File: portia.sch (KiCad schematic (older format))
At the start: 60 parts, among them J1 USB_B_Micro, J11 Conn_01x02, J12 Conn_01x02, J13 Conn_01x02, J14 Conn_01x02, J2 Conn_02x04_Counter_Clockwise, J3 Conn_01x02, J4 Conn_01x02, J5 RASPBERRYPI-40-PIN-GPIO, J7 Conn_01x02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

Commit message: modified trace connections
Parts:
- removed D8: D, Diode_SMD:D_SOD-123F, symbol Device:D
- removed JP8, JP9: SolderJumper_2_Open, Jumper:SolderJumper-2_P1.3mm_Open_RoundedPad1.0x1.5mm, symbol Jumper:SolderJumper_2_Open
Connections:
- wire segments 221 -> 218
- no-connect marks 40 -> 42
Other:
- moved on the sheet: R16
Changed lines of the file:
@@
 EESchema Schematic File Version 4
-LIBS:esp32_io_board-cache
+LIBS:portia-cache
 EELAYER 26 0
 EELAYER END
@@
 	14950 7800 14600 7800
 $Comp
-L power:+3.3V #PWR0134
-U 1 1 5C5CAF79
-P 14150 7800
-F 0 "#PWR0134" H 14150 7650 50  0001 C CNN
-F 1 "+3.3V" V 14165 7928 50  0000 L CNN
-F 2 "" H 14150 7800 50  0001 C CNN
-F 3 "" H 14150 7800 50  0001 C CNN
-	1    14150 7800
-	0    -1   -1   0
-$EndComp
-$Comp
 L Mechanical:MountingHole H4
 U 1 1 5C6145C5
@@
 	1    0    0    -1
 $EndComp
-$Comp
-L Device:D D8
-U 1 1 5C220000
-P 14450 7800
-F 0 "D8" H 14450 7584 50  0000 C CNN
-F 1 "D" H 14450 7675 50  0000 C CNN
-F 2 "Diode_SMD:D_SOD-123F" H 14450 7800 50  0001 C CNN
-F 3 "~" H 14450 7800 50  0001 C CNN
-	1    14450 7800
-	-1   0    0    1
-$EndComp
-Wire Wire Line
-	14150 7800 14300 7800
 Wire Wire Line
 	13850 8550 13850 8100
@@
 	13550 9450 13400 9450
 Wire Wire Line
-	13400 9450 13400 8950
-Wire Wire Line
-	12300 8950 12700 8950
-Wire Wire Line
-	13450 9050 13450 9550
+	13400 9450 13400 9150
+Wire Wire Line
+	13450 9050 13450 9300
 Wire Wire Line
 	13450 9550 13550 9550
@@
 	-1   0    0    1
 $EndComp
-Connection ~ 13450 9050
 Wire Wire Line
 	13400 8950 13600 8950
-Connection ~ 13400 8950
 Wire Wire Line
 	13450 9050 13600 9050
@@
 Text Label 16450 9700 0    50   ~ 0
 id_sda
-$Comp
-L Jumper:SolderJumper_2_Open JP8
-U 1 1 5C387087
-P 13000 8950
-F 0 "JP8" H 12954 9018 50  0000 L CNN
-F 1 "SolderJumper_2_Open" H 14200 10850 50  0000 L CNN
-F 2 "Jumper:SolderJumper-2_P1.3mm_Open_RoundedPad1.0x1.5mm" H 13000 8950 50  0001 C CNN
-F 3 "~" H 13000 8950 50  0001 C CNN
-	1    13000 8950
-	-1   0    0    1
-$EndComp
-Wire Wire Line
-	13150 8950 13400 8950
-Wire Wire Line
-	13150 9050 13450 9050
-$Comp
-L Jumper:SolderJumper_2_Open JP9
-U 1 1 5C3A9876
-P 13000 9050
-F 0 "JP9" H 12954 9118 50  0000 L CNN
-F 1 "SolderJumper_2_Open" H 14200 10750 50  0000 L CNN
-F 2 "Jumper:SolderJumper-2_P1.3mm_Open_RoundedPad1.0x1.5mm" H 13000 9050 50  0001 C CNN
-F 3 "~" H 13000 9050 50  0001 C CNN
-	1    13000 9050
-	-1   0    0    1
-$EndComp
 NoConn ~ 15050 8300
 NoConn ~ 15050 8500
@@
 Connection ~ 13950 9800
 Wire Wire Line
-	13950 9800 13950 9950
+	13950 9800 13950 9900
 Wire Wire Line
 	13150 8850 14200 8850
@@
 	8300 7400 8300 7650
 Wire Wire Line
-	12700 8950 12700 9350
-Wire Wire Line
-	12300 9050 12800 9050
-Connection ~ 12700 8950
-Wire Wire Line
-	12700 8950 12850 8950
-Wire Wire Line
-	12800 9050 12800 9250
-Connection ~ 12800 9050
-Wire Wire Line
-	12800 9050 12850 9050
-$Comp
-L Device:R_Small R16
-U 1 1 5C2A3FD8
-P 12800 9350
-F 0 "R16" V 12604 9350 50  0000 C CNN
-F 1 "R_Small" V 12695 9350 50  0000 C CNN
-F 2 "Resistor_SMD:R_0603_1608Metric" H 12800 9350 50  0001 C CNN
-F 3 "~" H 12800 9350 50  0001 C CNN
-	1    12800 9350
-	-1   0    0    1
-$EndComp
-$Comp
-L Device:R_Small R15
-U 1 1 5C2EA332
-P 12700 9450
-F 0 "R15" V 12504 9450 50  0000 C CNN
-F 1 "R_Small" V 12595 9450 50  0000 C CNN
-F 2 "Resistor_SMD:R_0603_1608Metric" H 12700 9450 50  0001 C CNN
-F 3 "~" H 12700 9450 50  0001 C CNN
-	1    12700 9450
-	-1   0    0    1
-$EndComp
-Wire Wire Line
-	12550 9550 12550 9650
-Wire Wire Line
-	12700 9550 12550 9550
-Connection ~ 12550 9550
-Wire Wire Line
-	12800 9450 12800 9650
-Wire Wire Line
-	12800 9650 12550 9650
-Connection ~ 12550 9650
-Wire Wire Line
-	12550 9650 12550 9800
-Wire Wire Line
 	10950 7850 10950 7500
 Connection ~ 10950 7850
@@
 $EndComp
 $Comp
-L power:GND #PWR?
+L power:GND #PWR0119
 U 1 1 5C438DC8
 P 14450 9150
-F 0 "#PWR?" H 14450 8900 50  0001 C CNN
+F 0 "#PWR0119" H 14450 8900 50  0001 C CNN
 F 1 "GND" V 14455 9022 50  0000 R CNN
 F 2 "" H 14450 9150 50  0001 C CNN
@@
 Wire Wire Line
 	14350 9150 14450 9150
+$Comp
+L Device:R_Small R16
+U 1 1 5C2A3FD8
+P 13200 9300
+F 0 "R16" V 13004 9300 50  0000 C CNN
+F 1 "R_Small" V 13095 9300 50  0000 C CNN
+F 2 "Resistor_SMD:R_0603_1608Metric" H 13200 9300 50  0001 C CNN
+F 3 "~" H 13200 9300 50  0001 C CNN
+	1    13200 9300
+	0    -1   -1   0
+$EndComp
+$Comp
+L Device:R_Small R15
+U 1 1 5C2E4AA2
+P 13200 9150
+F 0 "R15" V 13004 9150 50  0000 C CNN
+F 1 "R_Small" V 13095 9150 50  0000 C CNN
+F 2 "Resistor_SMD:R_0603_1608Metric" H 13200 9150 50  0001 C CNN
+F 3 "~" H 13200 9150 50  0001 C CNN
+	1    13200 9150
+	0    -1   -1   0
+$EndComp
+Wire Wire Line
+	12550 9550 12550 9800
+Wire Wire Line
+	13300 9150 13400 9150
+Connection ~ 13400 9150
+Wire Wire Line
+	13400 9150 13400 8950
+Wire Wire Line
+	13300 9300 13450 9300
+Connection ~ 13450 9300
+Wire Wire Line
+	13450 9300 13450 9550
+Wire Wire Line
+	13100 9150 13050 9150
+Wire Wire Line
+	13100 9300 13050 9300
+Wire Wire Line
+	13050 9150 13050 9300
+Wire Wire Line
+	13050 9900 13950 9900
+Connection ~ 13050 9300
+Wire Wire Line
+	13050 9300 13050 9900
+Connection ~ 13950 9900
+Wire Wire Line
+	13950 9900 13950 9950
+NoConn ~ 12300 8950
+NoConn ~ 12300 9050
+$Comp
+L power:+3.3V #PWR0134
+U 1 1 5C5CAF79
+P 14600 7800
+F 0 "#PWR0134" H 14600 7650 50  0001 C CNN
+F 1 "+3.3V" V 14615 7928 50  0000 L CNN
+F 2 "" H 14600 7800 50  0001 C CNN
+F 3 "" H 14600 7800 50  0001 C CNN
+	1    14600 7800
+	0    -1   -1   0
+$EndComp
 $EndSCHEMATC

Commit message: resolved routing issue
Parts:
- J5: footprint SparkFun-Boards:2X20-SHROUDED -> Connector_PinSocket_2.54mm:PinSocket_2x20_P2.54mm_Vertical
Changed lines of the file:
@@
 F 0 "J5" H 15650 9865 50  0000 C CNN
 F 1 "RASPBERRYPI-40-PIN-GPIO" H 15650 9774 50  0000 C CNN
-F 2 "SparkFun-Boards:2X20-SHROUDED" H 15680 8750 20  0001 C CNN
+F 2 "Connector_PinSocket_2.54mm:PinSocket_2x20_P2.54mm_Vertical" H 15680 8750 20  0001 C CNN
 F 3 "" H 15650 8600 50  0001 C CNN
 	1    15650 8600

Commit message: redesign removed 40 pin header
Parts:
- removed J5: RASPBERRYPI-40-PIN-GPIO, Connector_PinSocket_2.54mm:PinSocket_2x20_P2.54mm_Vertical, symbol SparkFun-Boards:RASPBERRYPI-40-PIN-GPIO
- removed JP4, JP7: SolderJumper_2_Open, Jumper:SolderJumper-2_P1.3mm_Open_RoundedPad1.0x1.5mm, symbol Jumper:SolderJumper_2_Open
- removed R12, R15, R16: R_Small, Resistor_SMD:R_0603_1608Metric, symbol Device:R_Small
- removed U7: CAT24C256, Package_SO:SOIC-8-1EP_3.9x4.9mm_P1.27mm_EP2.35x2.35mm, symbol Memory_EEPROM:CAT24C256
- F1: footprint Fuse:Fuse_1812_4532Metric_Pad1.30x3.40mm_HandSolder -> Fuse:Fuse_1206_3216Metric_Pad1.42x1.75mm_HandSolder
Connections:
- net labels removed: id_clk, id_sda
- wire segments 218 -> 160
- no-connect marks 42 -> 26

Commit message: updated schematic redesign
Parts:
- removed J2: Conn_02x04_Counter_Clockwise, Connector_PinHeader_2.54mm:PinHeader_2x04_P2.54mm_Vertical, symbol Connector_Generic:Conn_02x04_Counter_Clockwise
- removed J4: Conn_01x02, Connector_PinHeader_2.54mm:PinHeader_1x02_P2.54mm_Vertical, symbol Connector_Generic:Conn_01x02
- removed SW2: Bootloader, Button_Switch_SMD:SW_SPST_EVPBF, symbol Switch:SW_Push
- added J10, J15, J2, J5, J6, J9: Conn_01x02, Connector_PinHeader_2.54mm:PinHeader_1x02_P2.54mm_Vertical, symbol Connector_Generic:Conn_01x02
- added J16, J4, J8: Conn_01x04, Connector_PinHeader_2.54mm:PinHeader_1x04_P2.54mm_Vertical, symbol Connector_Generic:Conn_01x04
- added M1: ISL29125, SparkFun-Sensors:ODFN-LD-6, symbol SparkFun-Sensors:ISL29125
- added R12, R15, R16, R17: R_Small, Resistor_SMD:R_0603_1608Metric, symbol Device:R_Small
- added U2: TMP102, SparkFun-Sensors:SOT563, symbol SparkFun-Sensors:TMP102
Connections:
- net GND: now also J15.2 (Pin_2), M1.3 (GND), U2.5 (VCC)
- net at U4.10 (IO25): now also J4.2 (Pin_2)
- net at U4.11 (IO26): now also J4.1 (Pin_1)
- net at U4.12 (IO27): now also J8.4 (Pin_4)
- net at U4.13 (IO14): now also J8.3 (Pin_3)
- net at U4.14 (IO12): now also J8.2 (Pin_2)
- net at U4.16 (IO13): now also J8.1 (Pin_1)
- net at U4.25 (IO0): now also J15.1 (Pin_1)
- net at U4.6 (IO34): now also J2.2 (Pin_2)
- net at U4.7 (IO35): now also J2.1 (Pin_1)
- net at U4.8 (IO32): now also J4.4 (Pin_4)
- net at U4.9 (IO33): now also J4.3 (Pin_3)
- net at U6.13 (SD4): now also R15.1, U2.6 (SDA)
- net at U6.14 (SC4): now also R17.1, U2.1 (SCL)
- net at U6.15 (SD5): now also M1.4 (SDA), R16.2
- net at U6.16 (SC5): now also M1.6 (SCL), R12.2
- net at U6.17 (SD6): now also J5.2 (Pin_2)
- net at U6.18 (SC6): now also J5.1 (Pin_1)
- net at U6.19 (SD7): now also J6.2 (Pin_2)
- net at U6.20 (SC7): now also J6.1 (Pin_1)
- net clk: no longer names the net of U4.30 (IO18)
- net clk: now also J16.3 (Pin_3)
- net cs: no longer names the net of U4.29 (IO5)
- net cs: now also J16.4 (Pin_4)
- net miso: no longer names the net of U4.31 (IO19)
- net miso: now also J16.2 (Pin_2)
- net mosi: no longer names the net of U4.37 (IO23)
- net mosi: now also J16.1 (Pin_1)
- net rx: no longer names the net of U4.27 (IO16)
- net rx: now also J10.2 (Pin_2)
- net scl0: no longer names the net of U4.36 (IO22)
- net scl0: now also J9.1 (Pin_1)
- net sda0: no longer names the net of U4.33 (IO21)
- net sda0: now also J9.2 (Pin_2)
- net tx: no longer names the net of U4.28 (IO17)
- net tx: now also J10.1 (Pin_1)
- new net 3.3V: M1.1 (VDD), R12.1, R15.2, R16.1, R17.2, U2.2 (GND)
- no-connect marks 26 -> 20

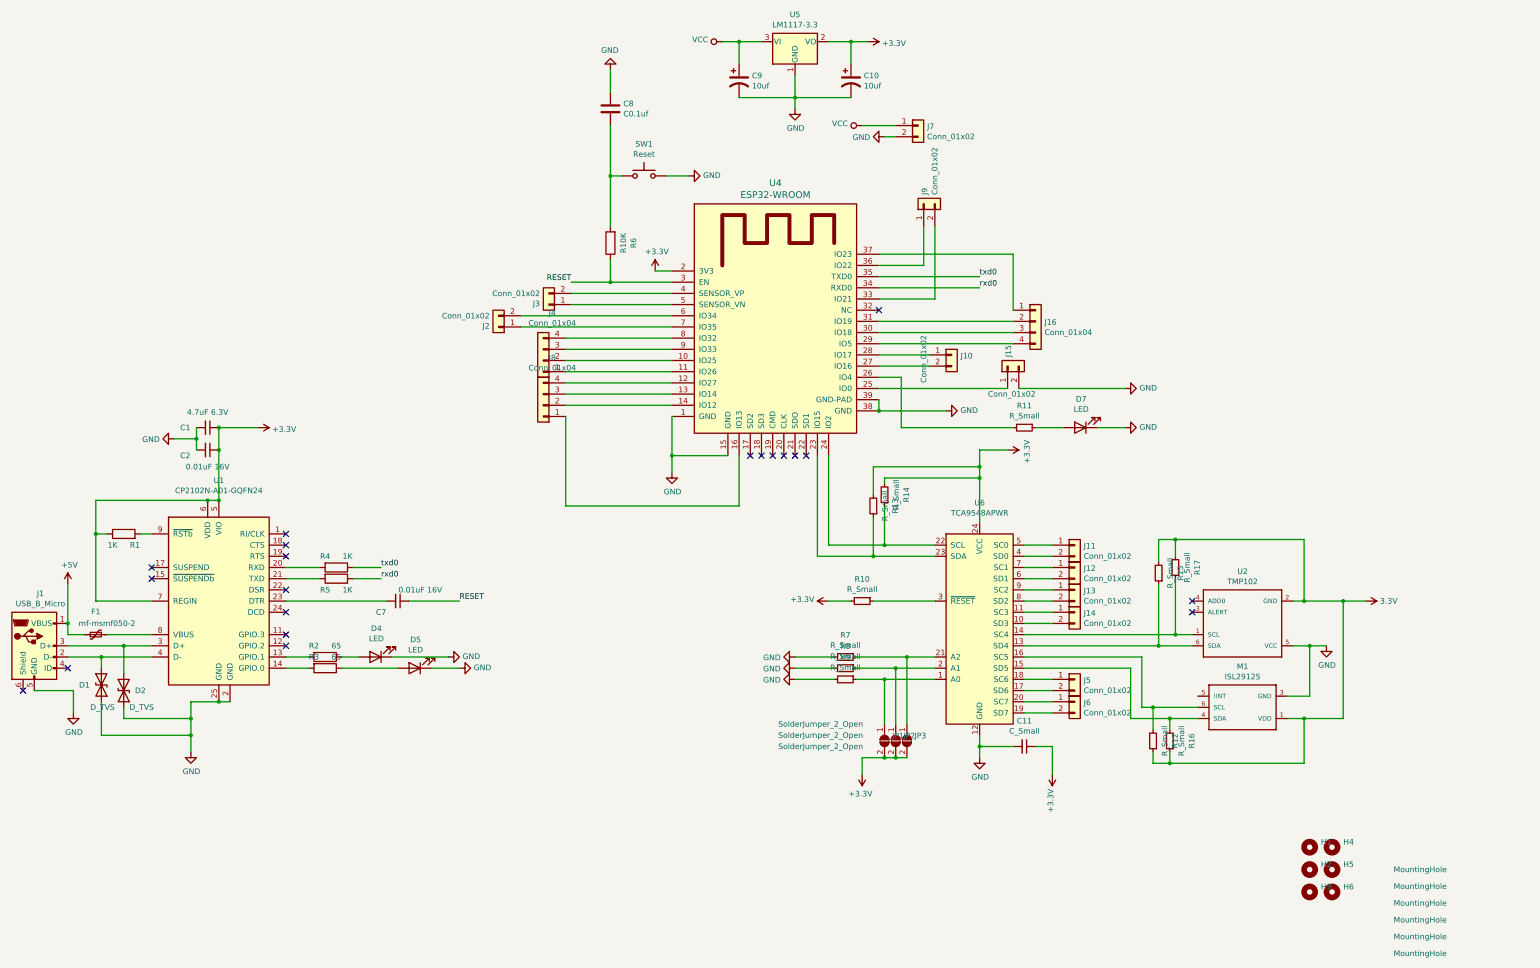
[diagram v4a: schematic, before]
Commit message: redesign layout sensors
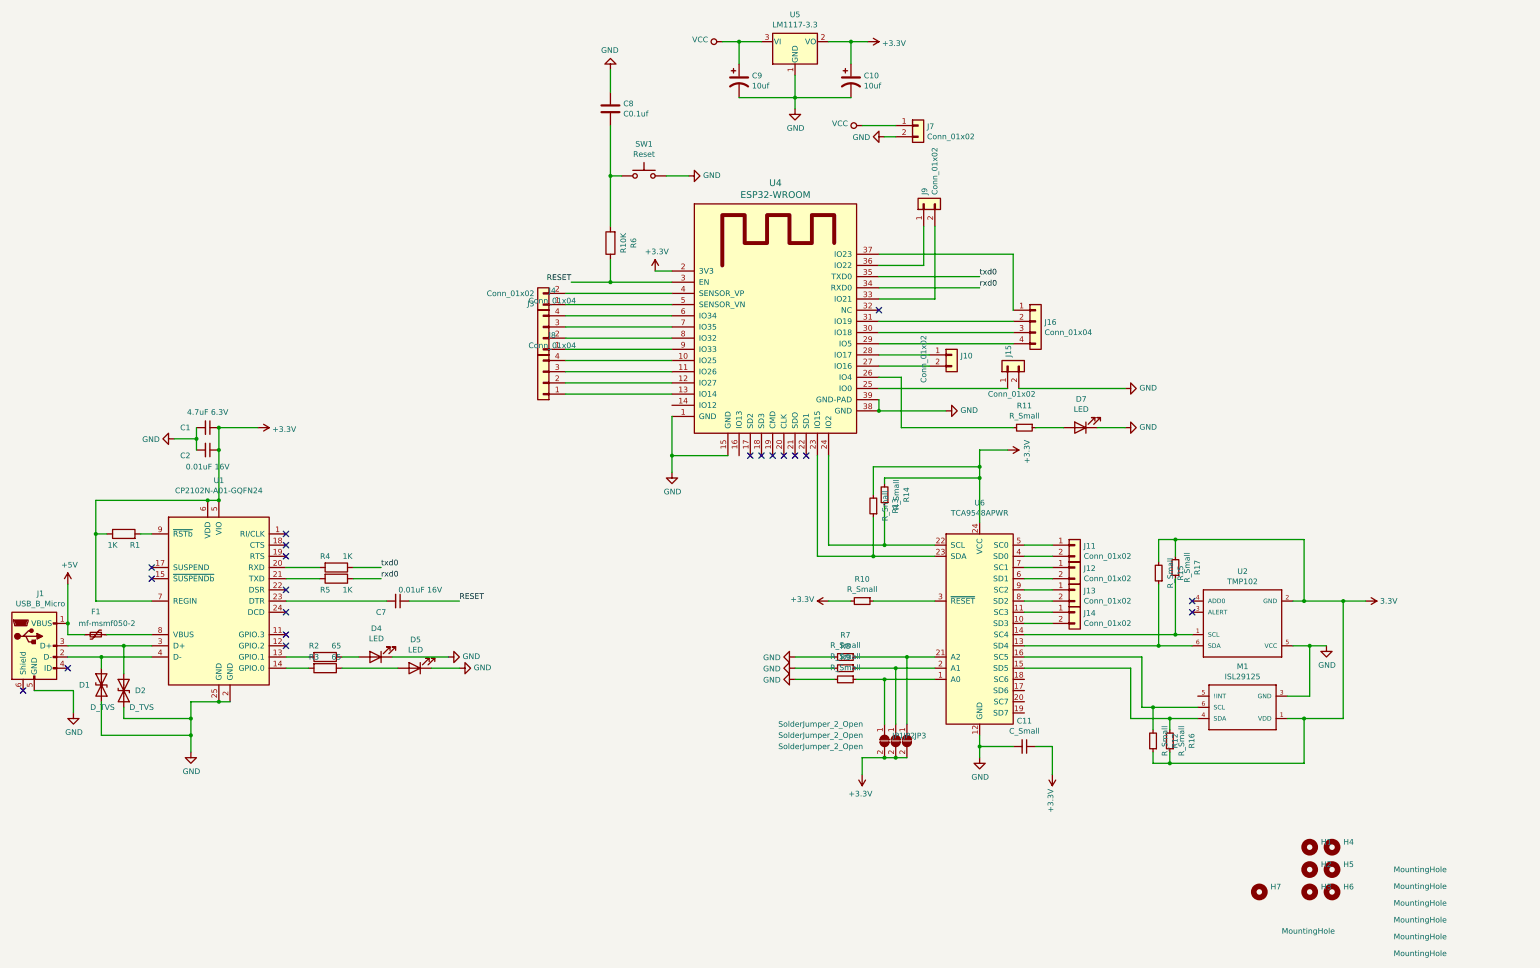
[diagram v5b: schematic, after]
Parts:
- removed J2, J5, J6: Conn_01x02, Connector_PinHeader_2.54mm:PinHeader_1x02_P2.54mm_Vertical, symbol Connector_Generic:Conn_01x02
- added H7: MountingHole, MountingHole:MountingHole_3mm, symbol Mechanical:MountingHole
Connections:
- net at U4.10 (IO25): now also J8.4 (Pin_4); no longer J4.2 (Pin_2)
- net at U4.11 (IO26): now also J8.3 (Pin_3); no longer J4.1 (Pin_1)
- net at U4.12 (IO27): now also J8.2 (Pin_2); no longer J8.4 (Pin_4)
- net at U4.13 (IO14): now also J8.1 (Pin_1); no longer J8.3 (Pin_3)
- net at U4.14 (IO12): no longer J8.2 (Pin_2)
- net at U4.16 (IO13): no longer J8.1 (Pin_1)
- net at U4.6 (IO34): now also J4.4 (Pin_4)
- net at U4.7 (IO35): now also J4.3 (Pin_3)
- net at U4.8 (IO32): now also J4.2 (Pin_2); no longer J4.4 (Pin_4)
- net at U4.9 (IO33): now also J4.1 (Pin_1); no longer J4.3 (Pin_3)
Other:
- moved on the sheet: J3, J4, J8
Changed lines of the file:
@@
 Wire Wire Line
 	12300 8450 12550 8450
-Wire Wire Line
-	9150 5500 8250 5500
-Wire Wire Line
-	9150 5600 8250 5600
 $Comp
 L Connector_Generic:Conn_01x02 J3
 U 1 1 5C5C727F
-P 8050 5600
-F 0 "J3" H 8130 5592 50  0000 L CNN
-F 1 "Conn_01x02" H 8130 5501 50  0000 L CNN
-F 2 "Connector_PinHeader_2.54mm:PinHeader_1x02_P2.54mm_Vertical" H 8050 5600 50  0001 C CNN
-F 3 "~" H 8050 5600 50  0001 C CNN
-	1    8050 5600
+P 8000 5600
+F 0 "J3" H 8080 5592 50  0000 L CNN
+F 1 "Conn_01x02" H 8080 5501 50  0000 L CNN
+F 2 "Connector_PinHeader_2.54mm:PinHeader_1x02_P2.54mm_Vertical" H 8000 5600 50  0001 C CNN
+F 3 "~" H 8000 5600 50  0001 C CNN
+	1    8000 5600
 	-1   0    0    1
 $EndComp
@@
 $EndComp
 Wire Wire Line
-	8200 6500 9150 6500
-Wire Wire Line
-	9750 6950 9750 7400
-Wire Wire Line
 	10950 7850 10950 7500
 Connection ~ 10950 7850
@@
 	13600 9700 14800 9700
 $Comp
-L Connector_Generic:Conn_01x02 J5
-U 1 1 5C503C93
-P 12750 8950
-F 0 "J5" H 12830 8942 50  0000 L CNN
-F 1 "Conn_01x02" H 12830 8851 50  0000 L CNN
-F 2 "Connector_PinHeader_2.54mm:PinHeader_1x02_P2.54mm_Vertical" H 12750 8950 50  0001 C CNN
-F 3 "~" H 12750 8950 50  0001 C CNN
-	1    12750 8950
-	1    0    0    -1
-$EndComp
-$Comp
-L Connector_Generic:Conn_01x02 J6
-U 1 1 5C50450C
-P 12750 9150
-F 0 "J6" H 12830 9142 50  0000 L CNN
-F 1 "Conn_01x02" H 12830 9051 50  0000 L CNN
-F 2 "Connector_PinHeader_2.54mm:PinHeader_1x02_P2.54mm_Vertical" H 12750 9150 50  0001 C CNN
-F 3 "~" H 12750 9150 50  0001 C CNN
-	1    12750 9150
-	1    0    0    -1
-$EndComp
-Wire Wire Line
-	12300 8950 12550 8950
-Wire Wire Line
-	12300 9050 12550 9050
-Wire Wire Line
-	12300 9150 12550 9150
-Wire Wire Line
-	12300 9250 12550 9250
-$Comp
 L Connector_Generic:Conn_01x02 J9
 U 1 1 5C544DE8
@@
 	0    -1   -1   0
 $EndComp
-$Comp
-L Connector_Generic:Conn_01x02 J2
-U 1 1 5C5879E7
-P 7600 5800
-F 0 "J2" H 7680 5792 50  0000 L CNN
-F 1 "Conn_01x02" H 7680 5701 50  0000 L CNN
-F 2 "Connector_PinHeader_2.54mm:PinHeader_1x02_P2.54mm_Vertical" H 7600 5800 50  0001 C CNN
-F 3 "~" H 7600 5800 50  0001 C CNN
-	1    7600 5800
-	-1   0    0    1
-$EndComp
-Wire Wire Line
-	7800 5700 9150 5700
-Wire Wire Line
-	7800 5800 9150 5800
 Wire Wire Line
 	8200 5900 9150 5900
@@
 L Connector_Generic:Conn_01x04 J4
 U 1 1 5C5D87D3
-P 8000 6100
-F 0 "J4" H 7920 5675 50  0000 C CNN
-F 1 "Conn_01x04" H 7920 5766 50  0000 C CNN
-F 2 "Connector_PinHeader_2.54mm:PinHeader_1x04_P2.54mm_Vertical" H 8000 6100 50  0001 C CNN
-F 3 "~" H 8000 6100 50  0001 C CNN
-	1    8000 6100
+P 8000 5900
+F 0 "J4" H 7920 5475 50  0000 C CNN
+F 1 "Conn_01x04" H 7920 5566 50  0000 C CNN
+F 2 "Connector_PinHeader_2.54mm:PinHeader_1x04_P2.54mm_Vertical" H 8000 5900 50  0001 C CNN
+F 3 "~" H 8000 5900 50  0001 C CNN
+	1    8000 5900
 	-1   0    0    1
 $EndComp
@@
 L Connector_Generic:Conn_01x04 J8
 U 1 1 5C5EC669
-P 8000 6500
-F 0 "J8" H 7920 6075 50  0000 C CNN
-F 1 "Conn_01x04" H 7920 6166 50  0000 C CNN
-F 2 "Connector_PinHeader_2.54mm:PinHeader_1x04_P2.54mm_Vertical" H 8000 6500 50  0001 C CNN
-F 3 "~" H 8000 6500 50  0001 C CNN
-	1    8000 6500
-	-1   0    0    1
-$EndComp
-Wire Wire Line
-	8200 6600 8200 7400
-Wire Wire Line
-	8200 7400 9750 7400
+P 8000 6300
+F 0 "J8" H 7920 5875 50  0000 C CNN
+F 1 "Conn_01x04" H 7920 5966 50  0000 C CNN
+F 2 "Connector_PinHeader_2.54mm:PinHeader_1x04_P2.54mm_Vertical" H 8000 6300 50  0001 C CNN
+F 3 "~" H 8000 6300 50  0001 C CNN
+	1    8000 6300
+	-1   0    0    1
+$EndComp
 $Comp
 L Connector_Generic:Conn_01x02 J15
@@
 	1    0    0    -1
 $EndComp
+Wire Wire Line
+	8200 5700 9150 5700
+Wire Wire Line
+	8200 5800 9150 5800
+Wire Wire Line
+	8200 5500 9150 5500
+Wire Wire Line
+	8200 5600 9150 5600
+$Comp
+L Mechanical:MountingHole H7
+U 1 1 5C3C0BB7
+P 14400 10850
+F 0 "H7" H 14500 10896 50  0000 L CNN
+F 1 "MountingHole" H 14600 10500 50  0000 L CNN
+F 2 "MountingHole:MountingHole_3mm" H 14400 10850 50  0001 C CNN
+F 3 "~" H 14400 10850 50  0001 C CNN
+	1    14400 10850
+	1    0    0    -1
+$EndComp
